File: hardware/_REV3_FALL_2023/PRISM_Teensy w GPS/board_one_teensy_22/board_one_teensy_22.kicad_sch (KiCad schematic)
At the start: 24 parts, among them J1 Micro_SD_Card_Det_Hirose_DM3AT, J3 3387, U1 Teensy4.0, U2 GPS-14414, U3 3966, U4 RFM69HCW_Breakout, U5 SFN-1407PA7.6

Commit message: Finished stepper implementation
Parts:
- added R6: 1k, Resistor_SMD:R_0603_1608Metric_Pad0.98x0.95mm_HandSolder, symbol Device:R
- C1, C2, C3: footprint Capacitor_SMD:C_0603_1608Metric -> Capacitor_SMD:C_0603_1608Metric_Pad1.08x0.95mm_HandSolder
- R1, R2, R3, R4, R5: footprint Resistor_SMD:R_0603_1608Metric -> Resistor_SMD:R_0603_1608Metric_Pad0.98x0.95mm_HandSolder
- Stepper1: value Conn_01x05_Socket -> Conn_01x03_Socket; footprint Connector_PinHeader_2.54mm:PinHeader_1x05_P2.54mm_Vertical -> Connector_PinHeader_2.54mm:PinHeader_1x03_P2.54mm_Vertical; symbol Connector:Conn_01x05_Socket -> Connector:Conn_01x03_Socket
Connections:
- net DIR: now also Stepper1.2 (Pin_2); no longer Stepper1.4 (Pin_4)
- net EN: no longer Stepper1.3 (Pin_3)
- net STEP: now also Stepper1.3 (Pin_3); no longer Stepper1.5 (Pin_5)
- net RX 4 renamed UART
- net UART: now also R6.2
- net TX 4: no longer names the net of U1.17
- net TX 4: now also R6.1; no longer Stepper1.2 (Pin_2)
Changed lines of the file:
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@@
   (junction (at 248.92 27.94) (diameter 0) (color 0 0 0 0)
+  )
+  (junction (at 94.615 82.55) (diameter 0) (color 0 0 0 0)
   )
   (junction (at 55.88 177.8) (diameter 0) (color 0 0 0 0)
@@
     (stroke (width 0) (type default))
   )
+  (wire (pts (xy 86.995 80.01) (xy 80.01 80.01))
+    (stroke (width 0) (type default))
+  )
   (wire (pts (xy 210.82 101.6) (xy 210.82 106.68))
     (stroke (width 0) (type default))
@@
     (stroke (width 0) (type default))
   )
+  (wire (pts (xy 94.615 82.55) (xy 94.615 80.01))
+    (stroke (width 0) (type default))
+  )
   (wire (pts (xy 46.355 160.02) (xy 55.88 160.02))
     (stroke (width 0) (type default))
@@
     (stroke (width 0) (type default))
   )
+  (wire (pts (xy 80.01 82.55) (xy 94.615 82.55))
+    (stroke (width 0) (type default))
+  )
   (wire (pts (xy 46.355 162.56) (xy 55.88 162.56))
     (stroke (width 0) (type default))
@@
   )
   (polyline (pts (xy 173.99 196.85) (xy 173.99 129.413))
+    (stroke (width 0) (type default))
+  )
+  (wire (pts (xy 94.615 82.55) (xy 99.695 82.55))
     (stroke (width 0) (type default))
   )
@@
     (effects (font (size 1.27 1.27)) (justify left bottom))
   )
+  (label "UART" (at 182.88 59.69 180) (fields_autoplaced)
+    (effects (font (size 1.27 1.27)) (justify right bottom))
+  )
   (label "5V" (at 227.33 27.94 0) (fields_autoplaced)
     (effects (font (size 1.27 1.27)) (justify left bottom))
@@
     (effects (font (size 1.27 1.27)) (justify right bottom))
   )
-  (label "TX 4" (at 182.88 59.69 180) (fields_autoplaced)
-    (effects (font (size 1.27 1.27)) (justify right bottom))
-  )
   (label "SCL" (at 246.38 105.41 180) (fields_autoplaced)
     (effects (font (size 1.27 1.27)) (justify right bottom))
@@
     (effects (font (size 1.27 1.27)) (justify right bottom))
   )
-  (label "RX 4" (at 80.01 82.55 0) (fields_autoplaced)
-    (effects (font (size 1.27 1.27)) (justify left bottom))
+  (label "DIR" (at 182.88 62.23 180) (fields_autoplaced)
+    (effects (font (size 1.27 1.27)) (justify right bottom))
   )
   (label "CONT 2" (at 44.45 64.77 180) (fields_autoplaced)
@@
     (effects (font (size 1.27 1.27)) (justify left bottom))
   )
-  (label "TX 4" (at 80.01 80.01 0) (fields_autoplaced)
-    (effects (font (size 1.27 1.27)) (justify left bottom))
-  )
   (label "MOSI" (at 46.355 172.72 180) (fields_autoplaced)
     (effects (font (size 1.27 1.27)) (justify right bottom))
@@
     (effects (font (size 1.27 1.27)) (justify right bottom))
   )
-  (label "EN" (at 182.88 62.23 180) (fields_autoplaced)
-    (effects (font (size 1.27 1.27)) (justify right bottom))
-  )
   (label "RX 5" (at 44.45 77.47 180) (fields_autoplaced)
     (effects (font (size 1.27 1.27)) (justify right bottom))
@@
     (effects (font (size 1.27 1.27)) (justify right bottom))
   )
-  (label "RX 4" (at 182.88 57.15 180) (fields_autoplaced)
-    (effects (font (size 1.27 1.27)) (justify right bottom))
-  )
   (label "Radio_RST" (at 44.45 80.01 180) (fields_autoplaced)
     (effects (font (size 1.27 1.27)) (justify right bottom))
@@
     (effects (font (size 1.27 1.27)) (justify right bottom))
   )
+  (label "UART" (at 99.695 82.55 0) (fields_autoplaced)
+    (effects (font (size 1.27 1.27)) (justify left bottom))
+  )
   (label "GND" (at 44.45 57.15 180) (fields_autoplaced)
     (effects (font (size 1.27 1.27)) (justify right bottom))
   )
-  (label "STEP" (at 182.88 67.31 180) (fields_autoplaced)
+  (label "STEP" (at 182.88 64.77 180) (fields_autoplaced)
     (effects (font (size 1.27 1.27)) (justify right bottom))
   )
   (label "PYRO 2" (at 44.45 69.85 180) (fields_autoplaced)
-    (effects (font (size 1.27 1.27)) (justify right bottom))
-  )
-  (label "DIR" (at 182.88 64.77 180) (fields_autoplaced)
     (effects (font (size 1.27 1.27)) (justify right bottom))
   )
@@
       (effects (font (size 1.27 1.27)))
     )
-    (property "Footprint" "Resistor_SMD:R_0603_1608Metric" (at 52.07 176.022 90)
+    (property "Footprint" "Resistor_SMD:R_0603_1608Metric_Pad0.98x0.95mm_HandSolder" (at 52.07 176.022 90)
       (effects (font (size 1.27 1.27)) hide)
     )
@@
       (effects (font (size 1.27 1.27)))
     )
-    (property "Footprint" "Resistor_SMD:R_0603_1608Metric" (at 52.07 173.482 90)
+    (property "Footprint" "Resistor_SMD:R_0603_1608Metric_Pad0.98x0.95mm_HandSolder" (at 52.07 173.482 90)
       (effects (font (size 1.27 1.27)) hide)
     )
@@
     )
   )
-  (symbol (lib_id "Connector:Conn_01x05_Socket") (at 187.96 62.23 0) (unit 1)
+  (symbol (lib_id "Connector:Conn_01x03_Socket") (at 187.96 62.23 0) (unit 1)
     (in_bom yes) (on_board yes) (dnp no) (fields_autoplaced)
     (property "Reference" "Stepper1" (at 189.23 60.96 0)
       (effects (font (size 1.27 1.27)) (justify left))
     )
-    (property "Value" "Conn_01x05_Socket" (at 189.23 63.5 0)
-      (effects (font (size 1.27 1.27)) (justify left))
-    )
-    (property "Footprint" "Connector_PinHeader_2.54mm:PinHeader_1x05_P2.54mm_Vertical" (at 187.96 62.23 0)
+    (property "Value" "Conn_01x03_Socket" (at 189.23 63.5 0)
+      (effects (font (size 1.27 1.27)) (justify left))
+    )
+    (property "Footprint" "Connector_PinHeader_2.54mm:PinHeader_1x03_P2.54mm_Vertical" (at 187.96 62.23 0)
       (effects (font (size 1.27 1.27)) hide)
     )
@@
     (pin "2")
     (pin "3")
-    (pin "4")
-    (pin "5")
     (instances
       (project "board_one_teensy_22"
@@
       (effects (font (size 1.27 1.27)) (justify left))
     )
-    (property "Footprint" "Capacitor_SMD:C_0603_1608Metric" (at 230.1748 34.29 0)
+    (property "Footprint" "Capacitor_SMD:C_0603_1608Metric_Pad1.08x0.95mm_HandSolder" (at 230.1748 34.29 0)
       (effects (font (size 1.27 1.27)) hide)
     )
@@
       (effects (font (size 1.27 1.27)) (justify left))
     )
-    (property "Footprint" "Resistor_SMD:R_0603_1608Metric" (at 187.452 92.71 90)
+    (property "Footprint" "Resistor_SMD:R_0603_1608Metric_Pad0.98x0.95mm_HandSolder" (at 187.452 92.71 90)
       (effects (font (size 1.27 1.27)) hide)
     )
@@
       (effects (font (size 1.27 1.27)) (justify left))
     )
-    (property "Footprint" "Resistor_SMD:R_0603_1608Metric" (at 187.452 106.68 90)
+    (property "Footprint" "Resistor_SMD:R_0603_1608Metric_Pad0.98x0.95mm_HandSolder" (at 187.452 106.68 90)
       (effects (font (size 1.27 1.27)) hide)
     )
@@
       (effects (font (size 1.27 1.27)) (justify left))
     )
-    (property "Footprint" "Capacitor_SMD:C_0603_1608Metric" (at 33.9598 163.83 0)
+    (property "Footprint" "Capacitor_SMD:C_0603_1608Metric_Pad1.08x0.95mm_HandSolder" (at 33.9598 163.83 0)
       (effects (font (size 1.27 1.27)) hide)
     )
@@
       (effects (font (size 1.27 1.27)))
     )
-    (property "Footprint" "Resistor_SMD:R_0603_1608Metric" (at 52.07 155.702 90)
+    (property "Footprint" "Resistor_SMD:R_0603_1608Metric_Pad0.98x0.95mm_HandSolder" (at 52.07 155.702 90)
       (effects (font (size 1.27 1.27)) hide)
     )
@@
         (path "/7a48c3b0-2761-409e-ae2f-7ebae3820225"
           (reference "R3") (unit 1)
+        )
+      )
+    )
+  )
+  (symbol (lib_id "Device:R") (at 90.805 80.01 90) (unit 1)
+    (in_bom yes) (on_board yes) (dnp no)
+    (property "Reference" "R6" (at 90.805 77.47 90)
+      (effects (font (size 1.27 1.27)))
+    )
+    (property "Value" "1k" (at 90.805 80.01 90)
+      (effects (font (size 1.27 1.27)))
+    )
+    (property "Footprint" "Resistor_SMD:R_0603_1608Metric_Pad0.98x0.95mm_HandSolder" (at 90.805 81.788 90)
+      (effects (font (size 1.27 1.27)) hide)
+    )
+    (property "Datasheet" "~" (at 90.805 80.01 0)
+      (effects (font (size 1.27 1.27)) hide)
+    )
+    (pin "1")
+    (pin "2")
+    (instances
+      (project "board_one_teensy_22"
+        (path "/7a48c3b0-2761-409e-ae2f-7ebae3820225"
+          (reference "R6") (unit 1)
         )
       )
@@
       (effects (font (size 1.27 1.27)) (justify left))
     )
-    (property "Footprint" "Capacitor_SMD:C_0603_1608Metric" (at 211.7852 101.6 0)
-      (effects (font (size 1.27 1.27)) hide)
-    )
+    (property "Footprint" "Capacitor_SMD:C_0603_1608Metric_Pad1.08x0.95mm_HandSolder" (at 211.7852 101.6 0)
+      (effects (font (size 1.27 1.27)) hide)
+    )

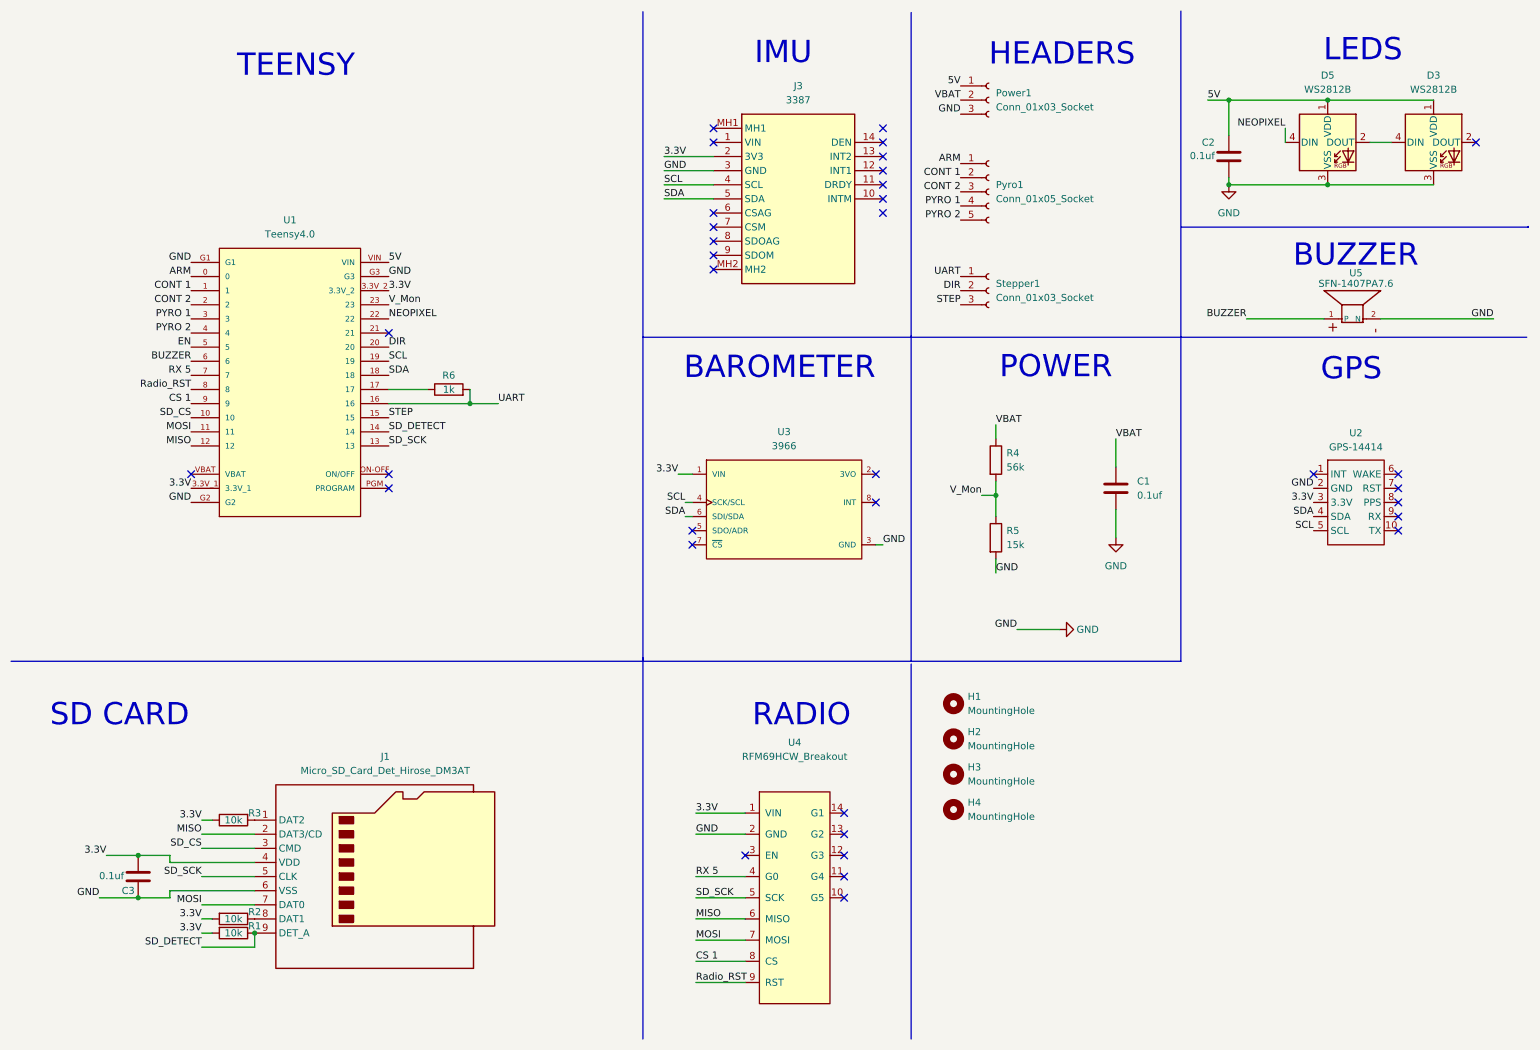
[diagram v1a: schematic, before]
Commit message: Add grounded mount on FC
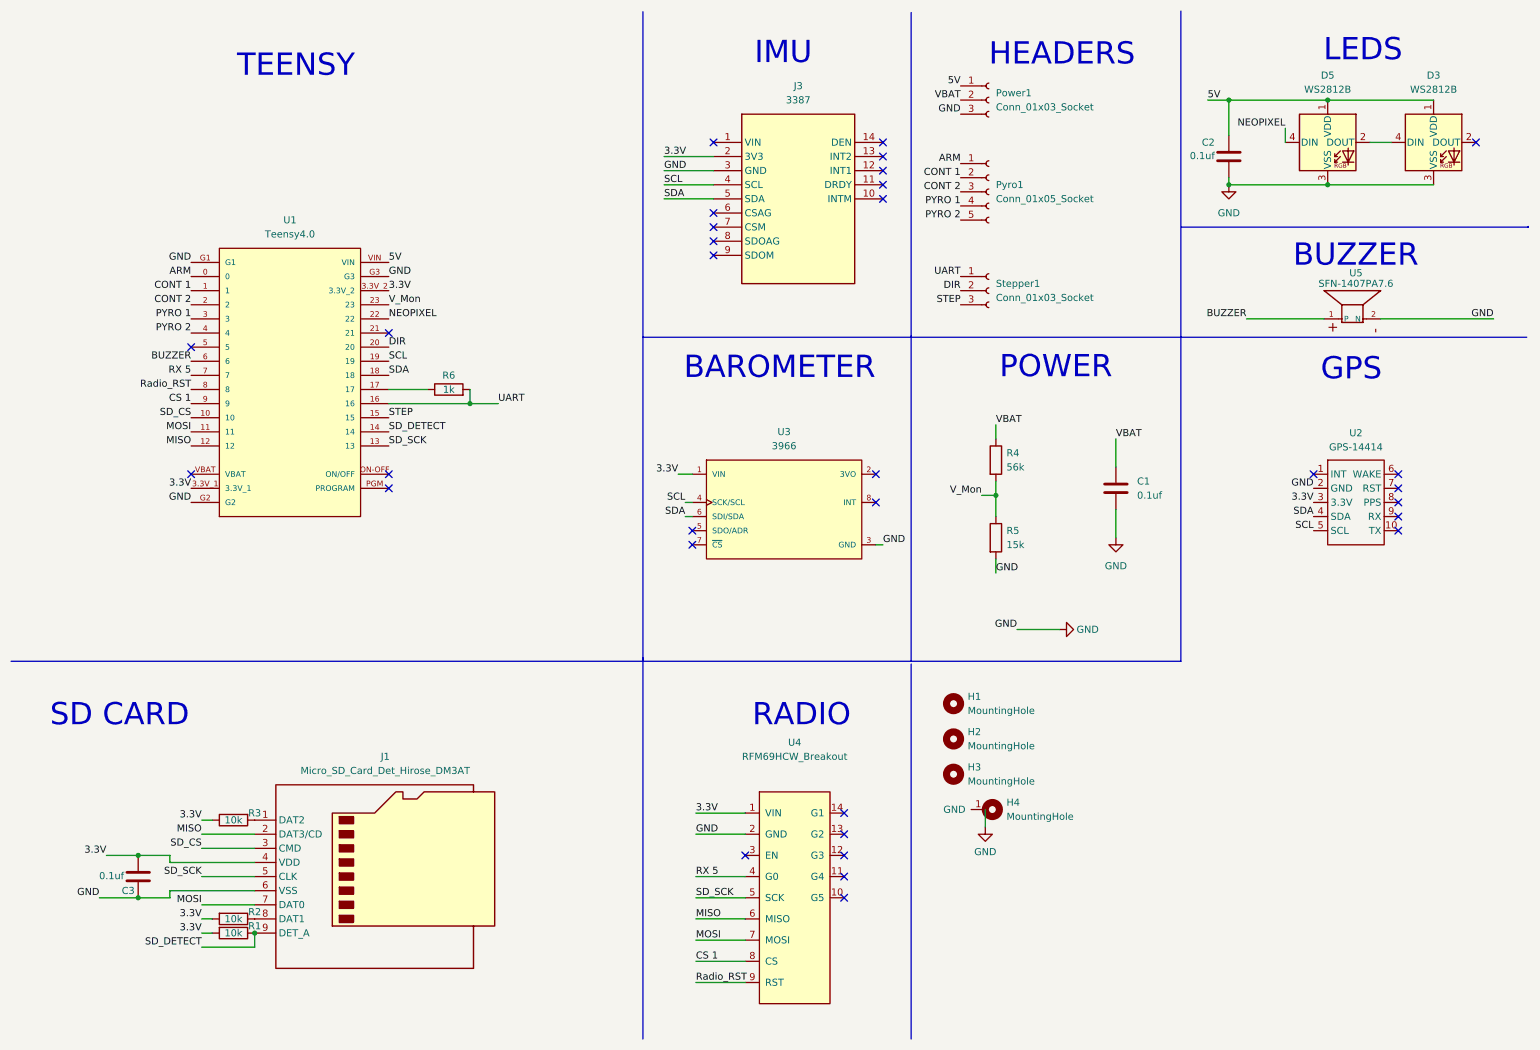
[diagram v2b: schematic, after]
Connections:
- net GND: now also H4.1 (GND)
- net EN: no longer names the net of U1.5
- no-connect marks 35 -> 32
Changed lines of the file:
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@@
   (no_connect (at 275.59 35.56))
   (no_connect (at 261.62 105.41))
-  (no_connect (at 168.91 33.02))
   (no_connect (at 44.45 95.25))
   (no_connect (at 246.38 95.25))
-  (no_connect (at 138.43 33.02))
   (no_connect (at 161.925 156.21))
   (no_connect (at 80.01 69.85))
@@
   (no_connect (at 134.62 105.41))
   (no_connect (at 134.62 107.95))
-  (no_connect (at 168.91 48.26))
   (no_connect (at 80.01 95.25))
   (no_connect (at 80.01 97.79))
   (no_connect (at 168.91 43.18))
+  (no_connect (at 44.45 72.39))
   (no_connect (at 161.925 171.45))
   (no_connect (at 168.91 40.64))
   (no_connect (at 168.91 45.72))
-  (no_connect (at 138.43 58.42))
   (no_connect (at 138.43 48.26))
   (no_connect (at 261.62 95.25))
@@
     (stroke (width 0) (type default))
   )
+  (wire (pts (xy 187.325 158.75) (xy 187.325 155.575))
+    (stroke (width 0) (type default))
+  )
   (wire (pts (xy 189.23 99.06) (xy 186.69 99.06))
     (stroke (width 0) (type default))
@@
   (label "SD_DETECT" (at 80.01 87.63 0) (fields_autoplaced)
     (effects (font (size 1.27 1.27)) (justify left bottom))
-  )
-  (label "EN" (at 44.45 72.39 180) (fields_autoplaced)
-    (effects (font (size 1.27 1.27)) (justify right bottom))
   )
   (label "ARM" (at 44.45 59.69 180) (fields_autoplaced)
@@
     )
   )
-  (symbol (lib_id "Mechanical:MountingHole") (at 181.61 155.575 0) (unit 1)
+  (symbol (lib_name "MountingHole_1") (lib_id "Mechanical:MountingHole") (at 188.595 155.575 0) (unit 1)
     (in_bom yes) (on_board yes) (dnp no)
-    (property "Reference" "H4" (at 184.15 154.305 0)
+    (property "Reference" "H4" (at 191.135 154.305 0)
       (effects (font (size 1.27 1.27)) (justify left))
     )
-    (property "Value" "MountingHole" (at 184.15 156.845 0)
+    (property "Value" "MountingHole" (at 191.135 156.845 0)
       (effects (font (size 1.27 1.27)) (justify left))
     )
-    (property "Footprint" "MountingHole:MountingHole_3.2mm_M3_DIN965_Pad_TopBottom" (at 181.61 155.575 0)
-      (effects (font (size 1.27 1.27)) hide)
-    )
-    (property "Datasheet" "~" (at 181.61 155.575 0)
-      (effects (font (size 1.27 1.27)))
-    )
+    (property "Footprint" "MountingHole:MountingHole_3.2mm_M3_DIN965_Pad_TopBottom" (at 188.595 155.575 0)
+      (effects (font (size 1.27 1.27)) hide)
+    )
+    (property "Datasheet" "~" (at 188.595 155.575 0)
+      (effects (font (size 1.27 1.27)))
+    )
+    (pin "1")
     (instances
       (project "board_one_teensy_22"
@@
     )
   )
+  (symbol (lib_id "power:GND") (at 187.325 158.75 0) (unit 1)
+    (in_bom yes) (on_board yes) (dnp no) (fields_autoplaced)
+    (property "Reference" "#PWR04" (at 187.325 165.1 0)
+      (effects (font (size 1.27 1.27)) hide)
+    )
+    (property "Value" "GND" (at 187.325 163.195 0)
+      (effects (font (size 1.27 1.27)))
+    )
+    (property "Footprint" "" (at 187.325 158.75 0)
+      (effects (font (size 1.27 1.27)) hide)
+    )
+    (property "Datasheet" "" (at 187.325 158.75 0)
+      (effects (font (size 1.27 1.27)) hide)
+    )
+    (pin "1")
+    (instances
+      (project "board_one_teensy_22"
+        (path "/7a48c3b0-2761-409e-ae2f-7ebae3820225"
+          (reference "#PWR04") (unit 1)
+        )
+      )
+    )
+  )
   (symbol (lib_id "3387:3387") (at 138.43 33.02 0) (unit 1)
     (in_bom yes) (on_board yes) (dnp no) (fields_autoplaced)
@@
     (pin "8")
     (pin "9")
-    (pin "MH1")
-    (pin "MH2")
-    (instances
-      (project "board_one_teensy_22"
+    (instances
+      (project "board_one_teensy_22"

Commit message: Add JLC part numbers to FC
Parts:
- R1, R2, R3: Vendor C25811 -> C25804
- R4: Vendor C25811 -> C23206
- R5: Vendor C23024 -> C22809
- R6: Vendor (none) -> C21190
- U5: Vendor (none) -> C360603
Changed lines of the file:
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@@
       (effects (font (size 1.27 1.27)) (justify bottom) hide)
+    )
+    (property "Vendor" "C360603" (at 253.365 64.77 90)
+      (effects (font (size 1.27 1.27)) hide)
     )
     (pin "1")
@@
       (effects (font (size 1.27 1.27)) hide)
     )
-    (property "Vendor" "C25811" (at 52.07 177.8 0)
+    (property "Vendor" "C25804" (at 52.07 177.8 0)
       (effects (font (size 1.27 1.27)) hide)
     )
@@
       (effects (font (size 1.27 1.27)) hide)
     )
-    (property "Vendor" "C25811" (at 52.07 175.26 0)
+    (property "Vendor" "C25804" (at 52.07 175.26 0)
       (effects (font (size 1.27 1.27)) hide)
     )
@@
       (effects (font (size 1.27 1.27)) hide)
     )
-    (property "Vendor" "C25811" (at 189.23 92.71 0)
+    (property "Vendor" "C23206" (at 189.23 92.71 0)
       (effects (font (size 1.27 1.27)) hide)
     )
@@
       (effects (font (size 1.27 1.27)) hide)
     )
-    (property "Vendor" "C23024" (at 189.23 106.68 0)
+    (property "Vendor" "C22809" (at 189.23 106.68 0)
       (effects (font (size 1.27 1.27)) hide)
     )
@@
       (effects (font (size 1.27 1.27)) hide)
     )
-    (property "Vendor" "C25811" (at 52.07 157.48 0)
+    (property "Vendor" "C25804" (at 52.07 157.48 0)
       (effects (font (size 1.27 1.27)) hide)
     )
@@
       (effects (font (size 1.27 1.27)) hide)
     )
+    (property "Vendor" "C21190" (at 90.805 80.01 90)
+      (effects (font (size 1.27 1.27)) hide)
+    )
